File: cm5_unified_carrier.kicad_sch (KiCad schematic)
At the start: 16 parts, among them J101 436500403, J102 484050003, J103 484050003, J104 PJ-102AH, J105 1050170001

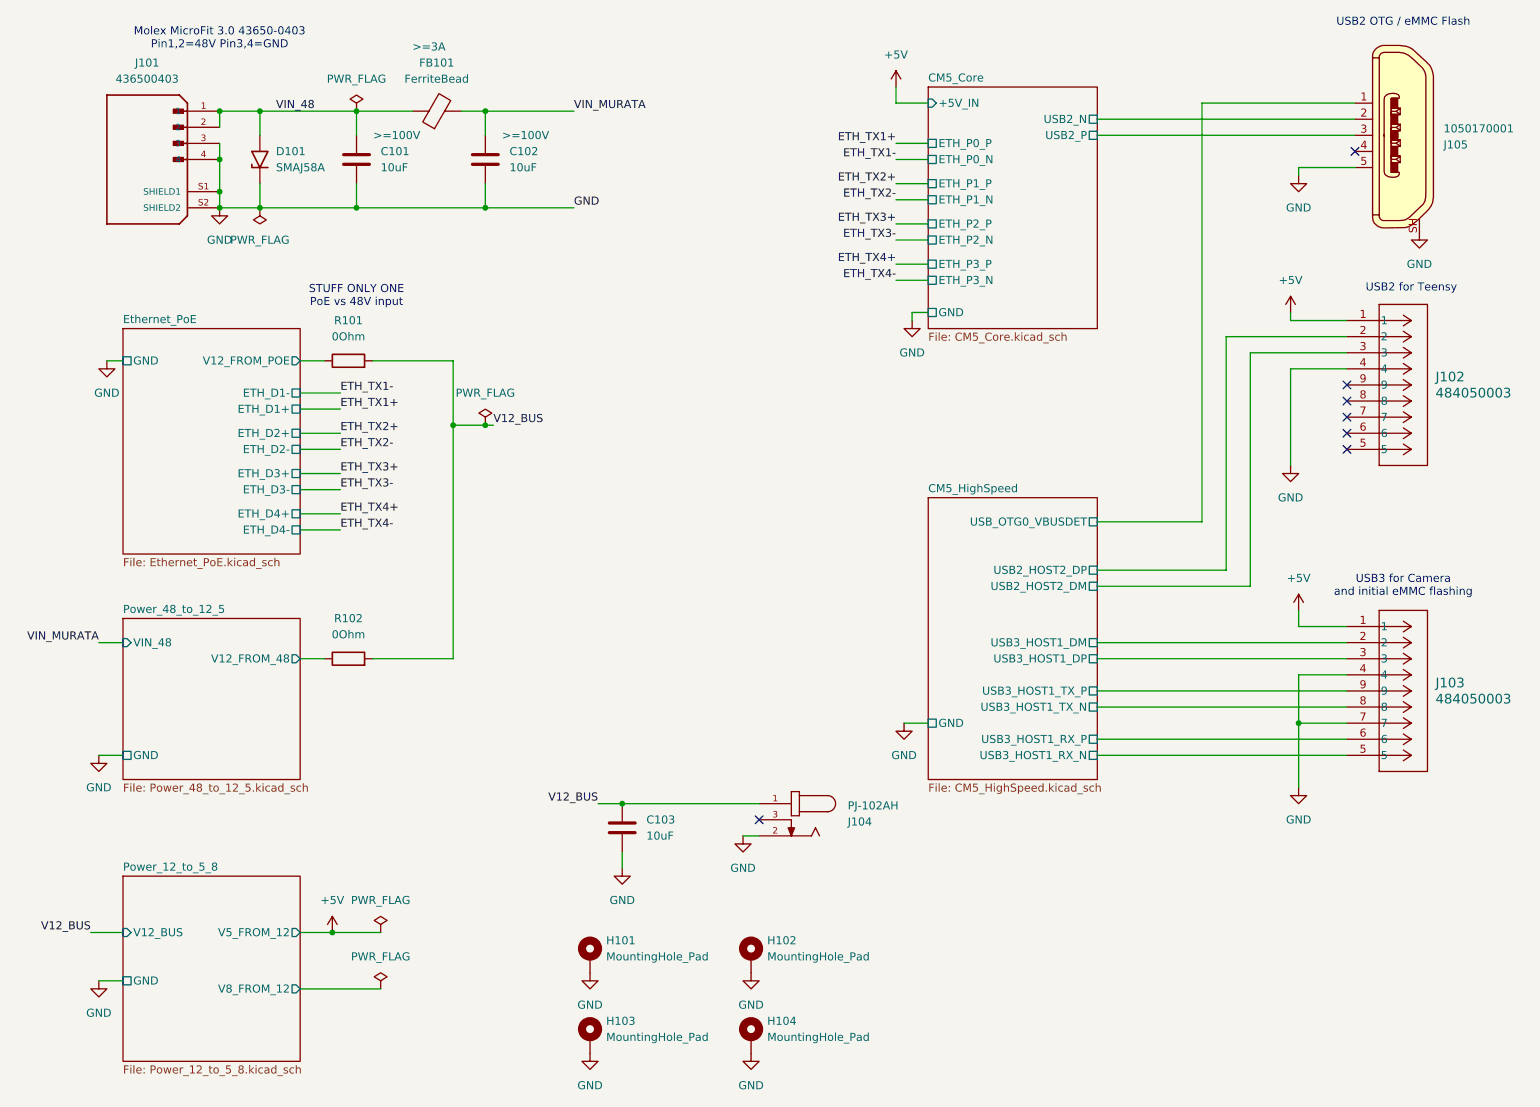
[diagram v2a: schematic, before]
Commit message: Update to fix power connection mistakes in both IWCD and HK configurations. For IWCD added bridge rectifier diodes needed for PoE, for HK updated to look at correct ref voltage for the 12V generation DC/DC, rotated the TVS to correct orientation and updated input diodes to be >=100V
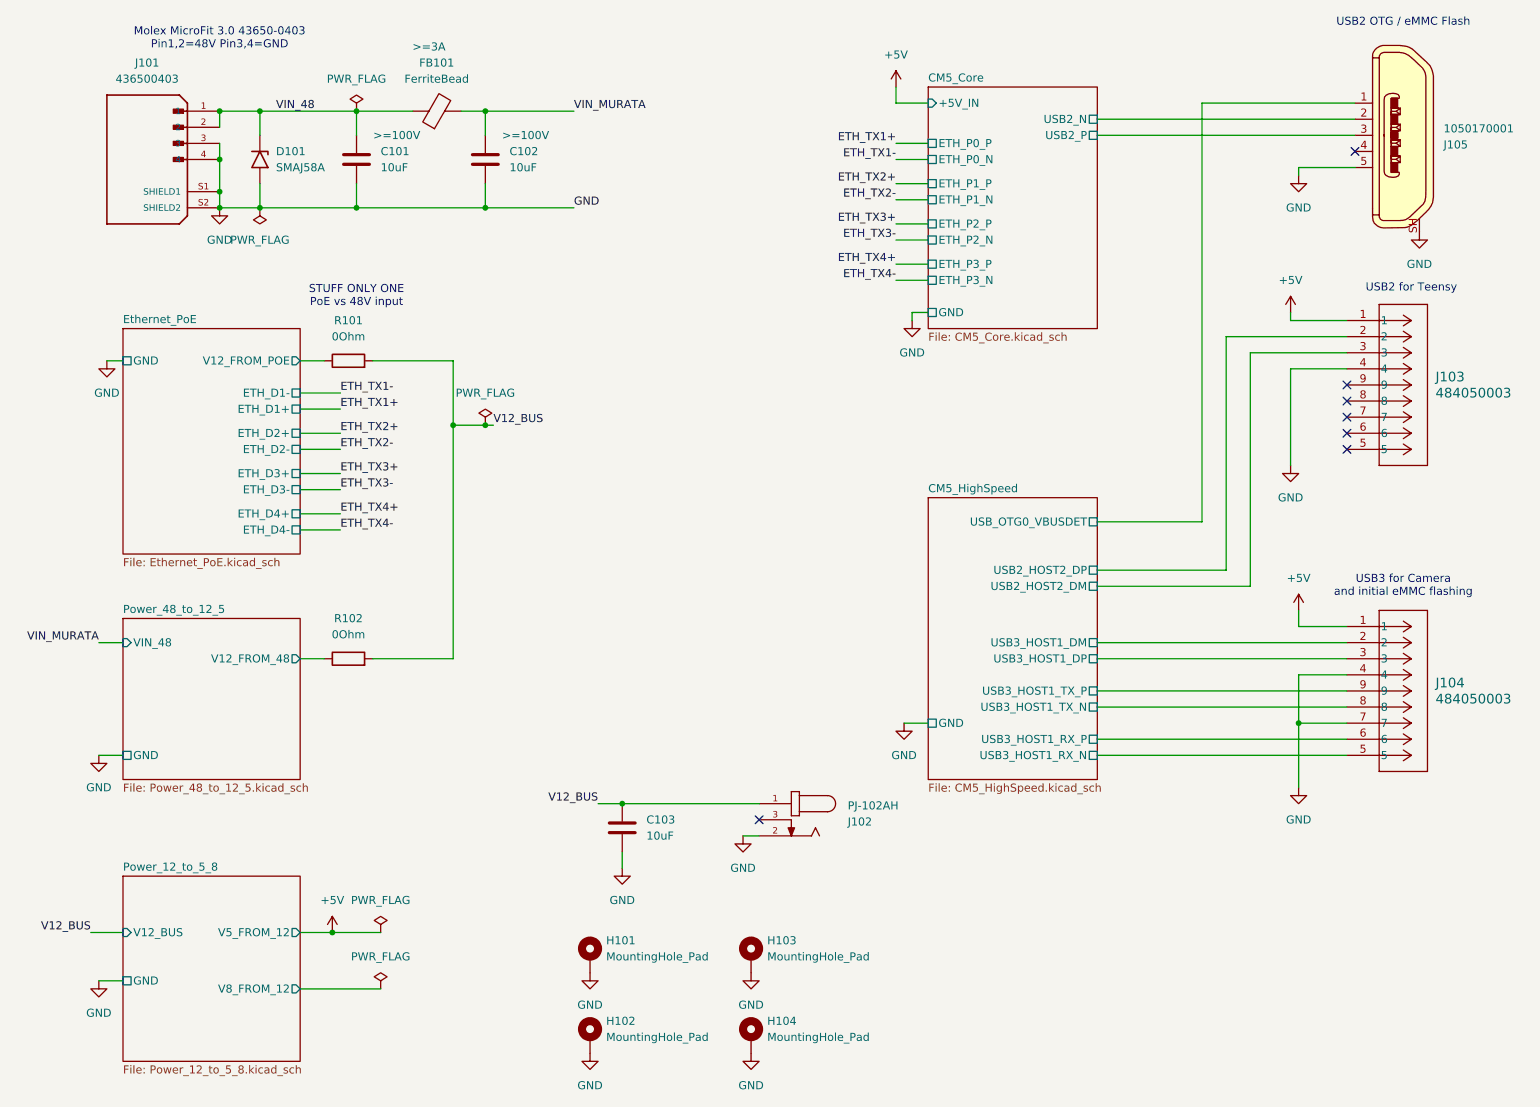
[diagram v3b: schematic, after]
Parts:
- renumbered H103 to H102, H102 to H103, J104 to J102, J102 to J103, J103 to J104
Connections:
- net GND: now also D101.2 (A2); no longer D101.1 (A1)
- net VIN_48: now also D101.1 (A1); no longer D101.2 (A2)
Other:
- moved on the sheet: D101
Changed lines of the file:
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@@
 		(dnp no)
 		(fields_autoplaced yes)
-		(property "Reference" "#PWR0104"
+		(property "Reference" "#PWR0102"
 			(at 26.67 181.61 0)
 			(effects
@@
 			(project "cm5_unified_carrier"
 				(path "/ee887ca3-c545-439a-9405-8d7a48a3d148"
-					(reference "#PWR0104")
+					(reference "#PWR0102")
 					(unit 1)
 				)
@@
 	(symbol
 		(lib_id "Diode:SMAJ58A")
-		(at 52.07 45.72 90)
+		(at 52.07 45.72 270)
 		(unit 1)
 		(exclude_from_sim no)
@@
 					(size 1.27 1.27)
 				)
-				(justify right)
+				(justify left)
 			)
 		)
@@
 					(size 1.27 1.27)
 				)
-				(justify right)
+				(justify left)
 			)
 		)
 		(property "Footprint" "Diode_SMD:D_SMA"
-			(at 57.15 45.72 0)
+			(at 46.99 45.72 0)
 			(effects
 				(font
@@
 		)
 		(property "Datasheet" "https://www.littelfuse.com/media?resourcetype=datasheets&itemid=75e32973-b177-4ee3-a0ff-cedaf1abdb93&filename=smaj-datasheet"
-			(at 52.07 46.99 0)
+			(at 52.07 44.45 0)
 			(effects
 				(font
@@
 		(dnp no)
 		(fields_autoplaced yes)
-		(property "Reference" "#PWR0105"
+		(property "Reference" "#PWR0113"
 			(at 153.67 140.97 0)
 			(effects
@@
 			(project ""
 				(path "/ee887ca3-c545-439a-9405-8d7a48a3d148"
-					(reference "#PWR0105")
+					(reference "#PWR0113")
 					(unit 1)
 				)
@@
 		(dnp no)
 		(fields_autoplaced yes)
-		(property "Reference" "#FLG0101"
+		(property "Reference" "#FLG0102"
 			(at 67.31 36.195 0)
 			(effects
@@
 			(project ""
 				(path "/ee887ca3-c545-439a-9405-8d7a48a3d148"
-					(reference "#FLG0101")
+					(reference "#FLG0102")
 					(unit 1)
 				)
@@
 		(dnp no)
 		(fields_autoplaced yes)
-		(property "Reference" "#PWR0108"
+		(property "Reference" "#PWR0118"
 			(at 215.9 120.65 0)
 			(effects
@@
 			(project "cm5_unified_carrier"
 				(path "/ee887ca3-c545-439a-9405-8d7a48a3d148"
-					(reference "#PWR0108")
+					(reference "#PWR0118")
 					(unit 1)
 				)
@@
 		(dnp no)
 		(fields_autoplaced yes)
-		(property "Reference" "#PWR0116"
+		(property "Reference" "#PWR0111"
 			(at 129.54 193.04 0)
 			(effects
@@
 			(project "cm5_unified_carrier"
 				(path "/ee887ca3-c545-439a-9405-8d7a48a3d148"
-					(reference "#PWR0116")
+					(reference "#PWR0111")
 					(unit 1)
 				)
@@
 		(dnp no)
 		(fields_autoplaced yes)
-		(property "Reference" "#PWR0121"
+		(property "Reference" "#PWR0120"
 			(at 234.95 63.5 0)
 			(effects
@@
 			(project "cm5_unified_carrier"
 				(path "/ee887ca3-c545-439a-9405-8d7a48a3d148"
-					(reference "#PWR0121")
+					(reference "#PWR0120")
 					(unit 1)
 				)
@@
 		(dnp no)
 		(fields_autoplaced yes)
-		(property "Reference" "#PWR0114"
+		(property "Reference" "#PWR0110"
 			(at 129.54 180.34 0)
 			(effects
@@
 			(project "cm5_unified_carrier"
 				(path "/ee887ca3-c545-439a-9405-8d7a48a3d148"
-					(reference "#PWR0114")
+					(reference "#PWR0110")
 					(unit 1)
 				)
@@
 		(dnp no)
 		(fields_autoplaced yes)
-		(property "Reference" "#PWR0120"
+		(property "Reference" "#PWR0117"
 			(at 215.9 54.61 0)
 			(effects
@@
 			(project "cm5_unified_carrier"
 				(path "/ee887ca3-c545-439a-9405-8d7a48a3d148"
-					(reference "#PWR0120")
+					(reference "#PWR0117")
 					(unit 1)
 				)
@@
 		(on_board yes)
 		(dnp no)
-		(property "Reference" "J104"
+		(property "Reference" "J102"
 			(at 144.78 150.1776 0)
 			(effects
@@
 			(project "cm5_unified_carrier"
 				(path "/ee887ca3-c545-439a-9405-8d7a48a3d148"
-					(reference "J104")
+					(reference "J102")
 					(unit 1)
 				)
@@
 		(dnp no)
 		(fields_autoplaced yes)
-		(property "Reference" "J103"
+		(property "Reference" "J104"
 			(at 237.49 128.2699 0)
 			(effects
@@
 			(project "cm5_unified_carrier"
 				(path "/ee887ca3-c545-439a-9405-8d7a48a3d148"
-					(reference "J103")
+					(reference "J104")
 					(unit 1)
 				)
@@
 		(dnp no)
 		(fields_autoplaced yes)
-		(property "Reference" "#PWR0110"
+		(property "Reference" "#PWR0116"
 			(at 214.63 100.33 0)
 			(effects
@@
 			(project "cm5_unified_carrier"
 				(path "/ee887ca3-c545-439a-9405-8d7a48a3d148"
-					(reference "#PWR0110")
+					(reference "#PWR0116")
 					(unit 1)
 				)
@@
 		(dnp no)
 		(fields_autoplaced yes)
-		(property "Reference" "#PWR0118"
+		(property "Reference" "#PWR0109"
 			(at 128.27 158.75 0)
 			(effects
@@
 			(project "cm5_unified_carrier"
 				(path "/ee887ca3-c545-439a-9405-8d7a48a3d148"
-					(reference "#PWR0118")
+					(reference "#PWR0109")
 					(unit 1)
 				)
@@
 		(dnp no)
 		(fields_autoplaced yes)
-		(property "Reference" "#FLG0105"
+		(property "Reference" "#FLG0101"
 			(at 52.07 55.245 0)
 			(effects
@@
 			(project "cm5_unified_carrier"
 				(path "/ee887ca3-c545-439a-9405-8d7a48a3d148"
-					(reference "#FLG0105")
+					(reference "#FLG0101")
 					(unit 1)
 				)
@@
 		(dnp no)
 		(fields_autoplaced yes)
-		(property "Reference" "#PWR0107"
+		(property "Reference" "#PWR0105"
 			(at 63.5 171.45 0)
 			(effects
@@
 			(project ""
 				(path "/ee887ca3-c545-439a-9405-8d7a48a3d148"
-					(reference "#PWR0107")
+					(reference "#PWR0105")
 					(unit 1)
 				)
@@
 		(dnp no)
 		(fields_autoplaced yes)
-		(property "Reference" "#PWR0102"
+		(property "Reference" "#PWR0103"
 			(at 27.94 83.82 0)
 			(effects
@@
 			(project "cm5_unified_carrier"
 				(path "/ee887ca3-c545-439a-9405-8d7a48a3d148"
-					(reference "#PWR0102")
+					(reference "#PWR0103")
 					(unit 1)
 				)
@@
 		(dnp no)
 		(fields_autoplaced yes)
-		(property "Reference" "H103"
+		(property "Reference" "H102"
 			(at 106.68 181.6099 0)
 			(effects
@@
 			(project "cm5_unified_carrier"
 				(path "/ee887ca3-c545-439a-9405-8d7a48a3d148"
-					(reference "H103")
+					(reference "H102")
 					(unit 1)
 				)
@@
 		(dnp no)
 		(fields_autoplaced yes)
-		(property "Reference" "#PWR0115"
+		(property "Reference" "#PWR0107"
 			(at 104.14 193.04 0)
 			(effects
@@
 			(project "cm5_unified_carrier"
 				(path "/ee887ca3-c545-439a-9405-8d7a48a3d148"
-					(reference "#PWR0115")
+					(reference "#PWR0107")
 					(unit 1)
 				)
@@
 		(dnp no)
 		(fields_autoplaced yes)
-		(property "Reference" "#PWR0113"
+		(property "Reference" "#PWR0106"
 			(at 104.14 180.34 0)
 			(effects
@@
 			(project "cm5_unified_carrier"
 				(path "/ee887ca3-c545-439a-9405-8d7a48a3d148"
-					(reference "#PWR0113")
+					(reference "#PWR0106")
 					(unit 1)
 				)
@@
 		(dnp no)
 		(fields_autoplaced yes)
-		(property "Reference" "#PWR0117"
+		(property "Reference" "#PWR0108"
 			(at 109.22 163.83 0)
 			(effects
@@
 			(project "cm5_unified_carrier"
 				(path "/ee887ca3-c545-439a-9405-8d7a48a3d148"
-					(reference "#PWR0117")
+					(reference "#PWR0108")
 					(unit 1)
 				)
@@
 		(dnp no)
 		(fields_autoplaced yes)
-		(property "Reference" "#PWR0109"
+		(property "Reference" "#PWR0115"
 			(at 214.63 73.66 0)
 			(effects
@@
 			(project "cm5_unified_carrier"
 				(path "/ee887ca3-c545-439a-9405-8d7a48a3d148"
-					(reference "#PWR0109")
+					(reference "#PWR0115")
 					(unit 1)
 				)
@@
 		(dnp no)
 		(fields_autoplaced yes)
-		(property "Reference" "H102"
+		(property "Reference" "H103"
 			(at 132.08 168.9099 0)
 			(effects
@@
 			(project "cm5_unified_carrier"
 				(path "/ee887ca3-c545-439a-9405-8d7a48a3d148"
-					(reference "H102")
+					(reference "H103")
 					(unit 1)
 				)
@@
 		(dnp no)
 		(fields_autoplaced yes)
-		(property "Reference" "J102"
+		(property "Reference" "J103"
 			(at 237.49 80.0099 0)
 			(effects
@@
 			(project ""
 				(path "/ee887ca3-c545-439a-9405-8d7a48a3d148"
-					(reference "J102")
+					(reference "J103")
 					(unit 1)
 				)
@@
 		(dnp no)
 		(fields_autoplaced yes)
-		(property "Reference" "#FLG0102"
+		(property "Reference" "#FLG0105"
 			(at 87.63 85.725 0)
 			(effects
@@
 			(project "cm5_unified_carrier"
 				(path "/ee887ca3-c545-439a-9405-8d7a48a3d148"
-					(reference "#FLG0102")
+					(reference "#FLG0105")
 					(unit 1)
 				)
@@
 		(dnp no)
 		(fields_autoplaced yes)
-		(property "Reference" "#PWR0106"
+		(property "Reference" "#PWR0119"
 			(at 215.9 151.13 0)
 			(effects
@@
 			(project "cm5_unified_carrier"
 				(path "/ee887ca3-c545-439a-9405-8d7a48a3d148"
-					(reference "#PWR0106")
+					(reference "#PWR0119")
 					(unit 1)
 				)
@@
 		(dnp no)
 		(fields_autoplaced yes)
-		(property "Reference" "#PWR0103"
+		(property "Reference" "#PWR0101"
 			(at 26.67 146.05 0)
 			(effects
@@
 			(project "cm5_unified_carrier"
 				(path "/ee887ca3-c545-439a-9405-8d7a48a3d148"
-					(reference "#PWR0103")
+					(reference "#PWR0101")
 					(unit 1)
 				)
@@
 		(dnp no)
 		(fields_autoplaced yes)
-		(property "Reference" "#PWR0101"
+		(property "Reference" "#PWR0104"
 			(at 45.72 59.69 0)
 			(effects
@@
 			(project ""
 				(path "/ee887ca3-c545-439a-9405-8d7a48a3d148"
-					(reference "#PWR0101")
+					(reference "#PWR0104")
 					(unit 1)
 				)
@@
 		(dnp no)
 		(fields_autoplaced yes)
-		(property "Reference" "#PWR0111"
+		(property "Reference" "#PWR0114"
 			(at 154.94 77.47 0)
 			(effects
@@
 			(project "cm5_unified_carrier"
 				(path "/ee887ca3-c545-439a-9405-8d7a48a3d148"
-					(reference "#PWR0111")
-					(unit 1)
-				)
+					(reference "#PWR0114")
+					(unit 1)
+				)
